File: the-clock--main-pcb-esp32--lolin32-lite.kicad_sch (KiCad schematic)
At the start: 14 parts, among them J1 Conn_01x04, SW1 SW_Push, SW2 SW_Push, SW3 SW_Push, SW4 SW_Push

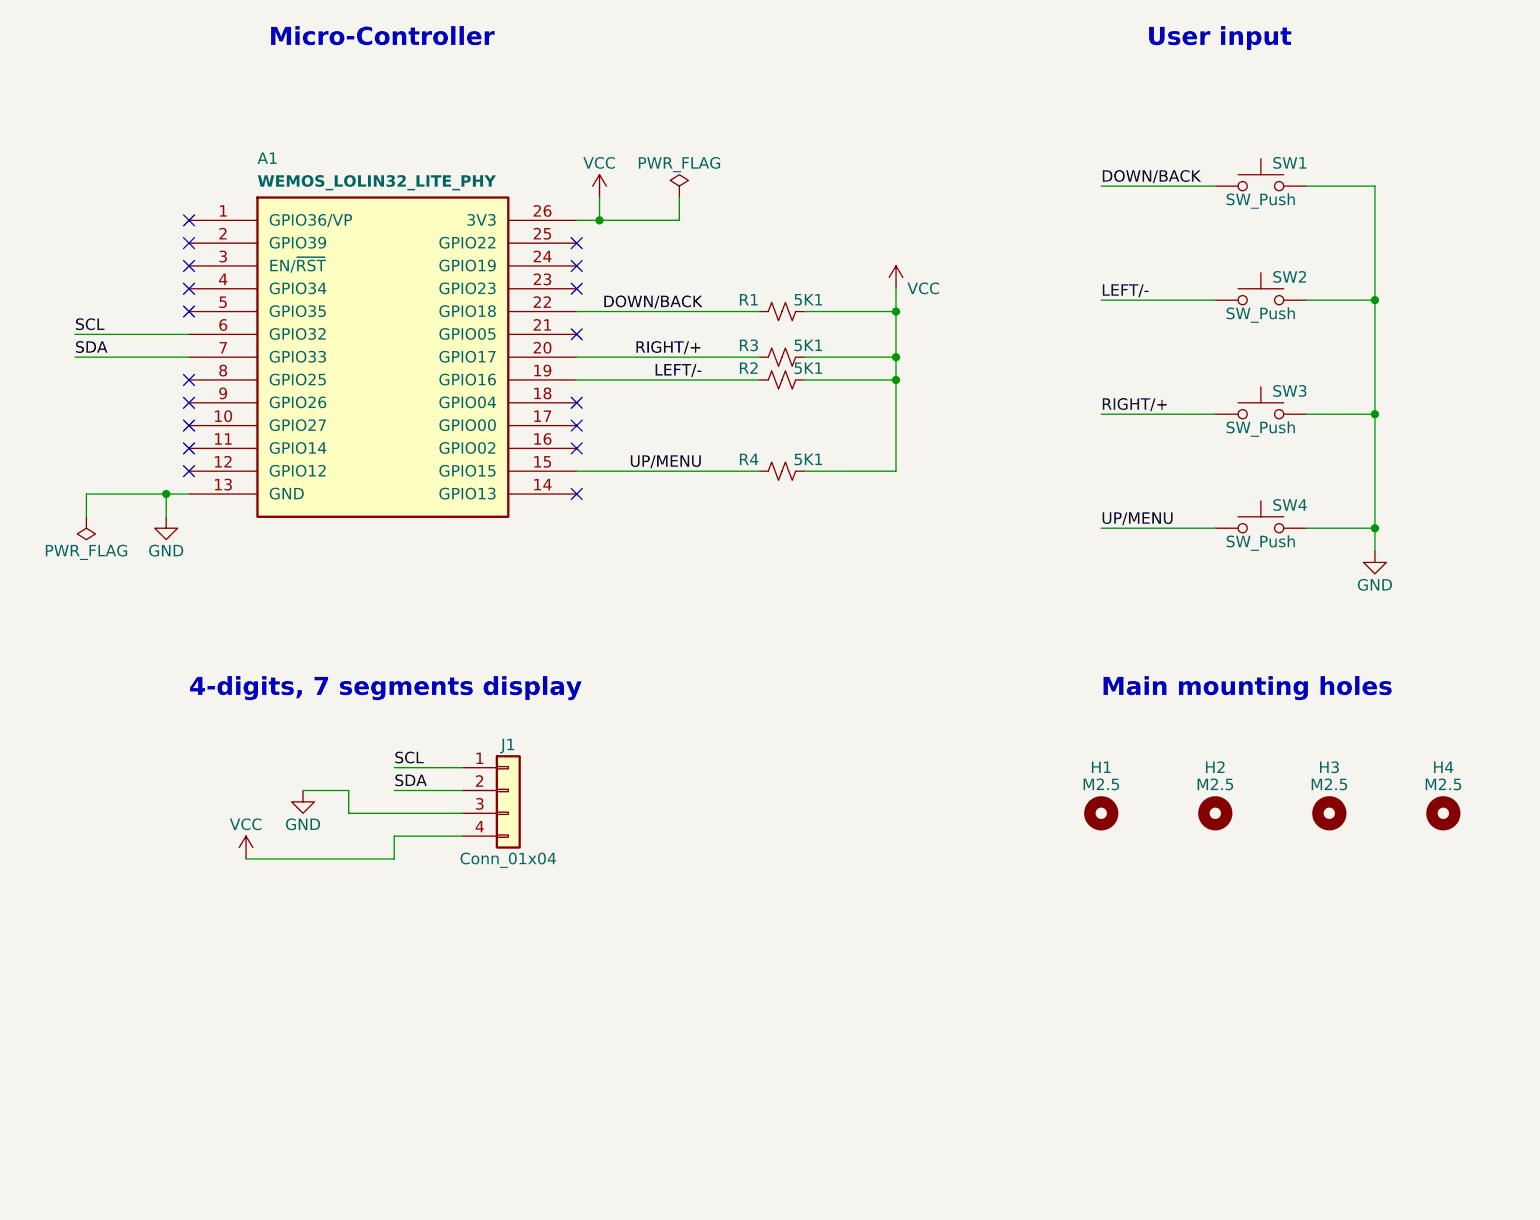
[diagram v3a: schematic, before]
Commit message: provision ambient light sensor
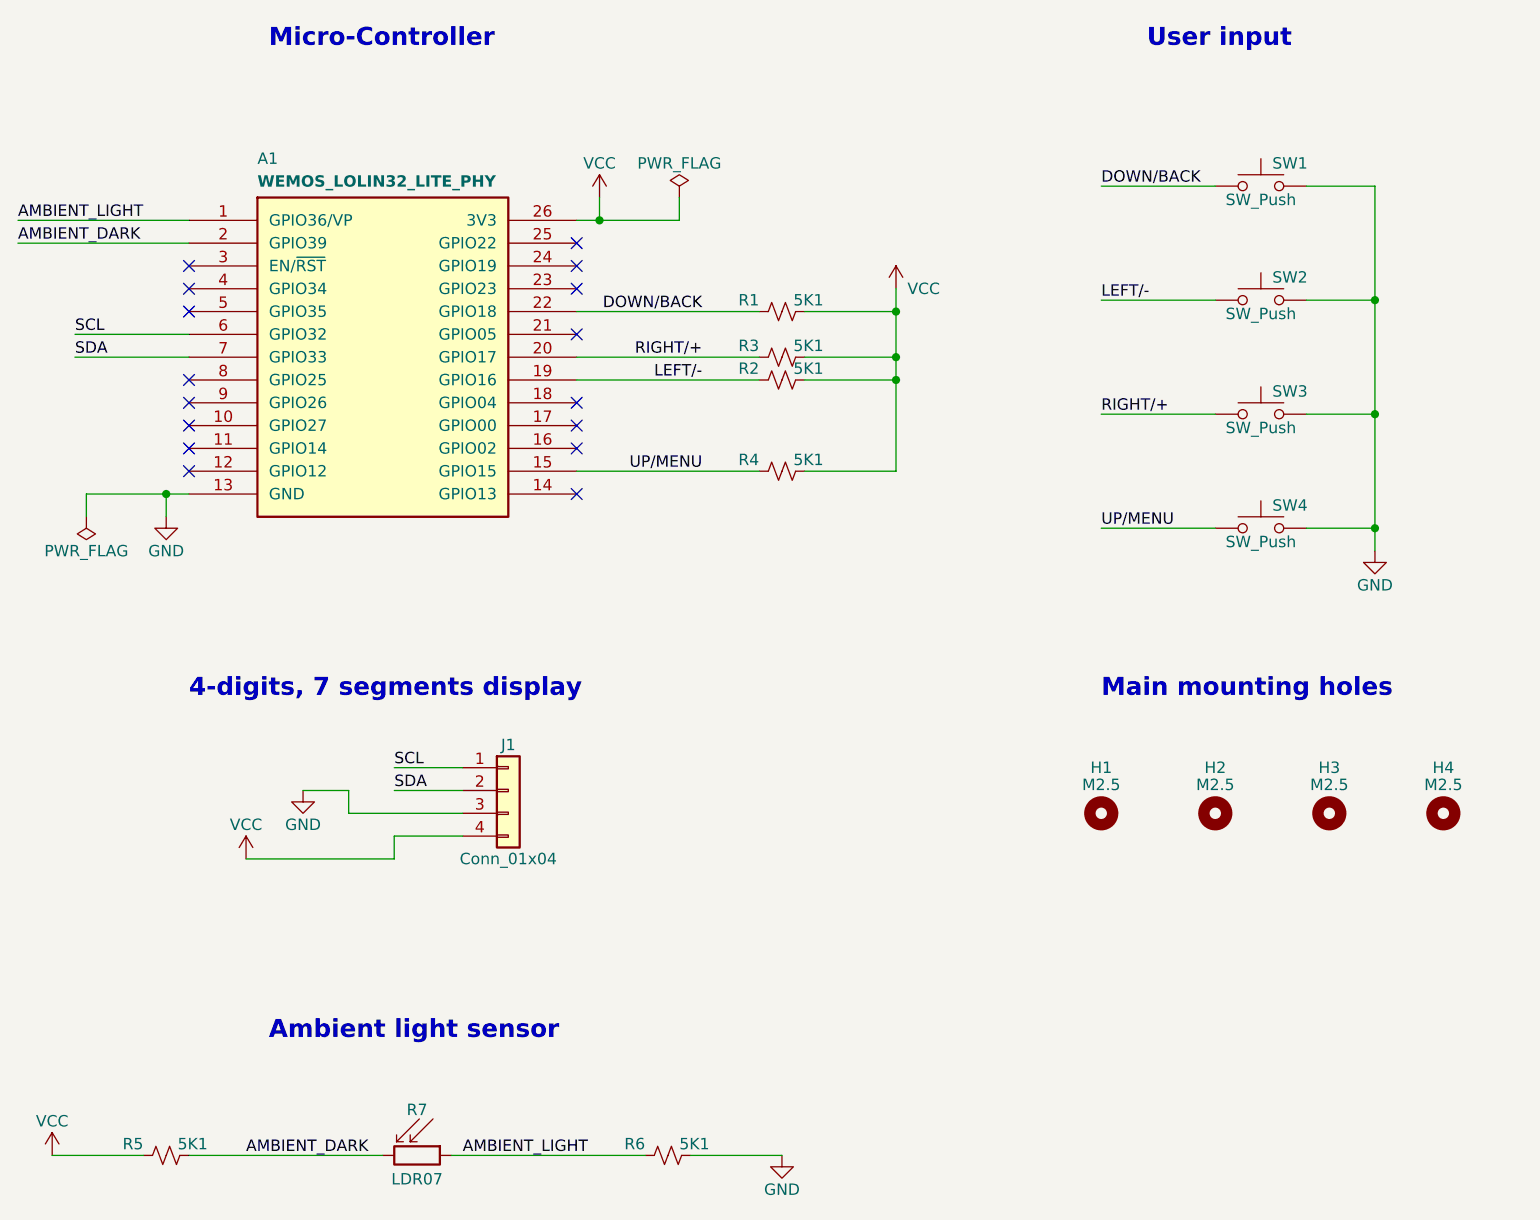
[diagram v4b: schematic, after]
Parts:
- added R5, R6: 5K1, commons-passives_THT:Passive_THT_resistor_W2.54mm_L10.16mm, symbol Device:R_Small_US
- added R7: LDR07, OptoDevice:R_LDR_5.1x4.3mm_P3.4mm_Vertical, symbol Sensor_Optical:LDR07
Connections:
- net GND: now also R6.2
- net VCC: now also R5.1
- net AMBIENT_LIGHT: now reaches A1.1 (GPIO36/VP)
- net AMBIENT_LIGHT: now also R6.1, R7.1
- net AMBIENT_DARK: now reaches A1.2 (GPIO39)
- net AMBIENT_DARK: now also R5.2, R7.2
- no-connect marks 18 -> 16
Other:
- note added: "Ambient light sensor"
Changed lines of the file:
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@@
   (no_connect (at 81.28 60.96))
   (no_connect (at 38.1 68.58))
-  (no_connect (at 38.1 50.8))
   (no_connect (at 81.28 71.12))
   (no_connect (at 38.1 55.88))
   (no_connect (at 38.1 76.2))
   (no_connect (at 81.28 53.34))
-  (no_connect (at 38.1 48.26))
   (no_connect (at 81.28 78.74))
   (no_connect (at 81.28 73.66))
@@
     (stroke (width 0) (type default))
   )
+  (wire (pts (xy 38.1 152.4) (xy 59.69 152.4))
+    (stroke (width 0) (type default))
+  )
   (wire (pts (xy 60.96 111.76) (xy 68.58 111.76))
     (stroke (width 0) (type default))
@@
     (stroke (width 0) (type default))
   )
+  (wire (pts (xy 19.05 50.8) (xy 38.1 50.8))
+    (stroke (width 0) (type default))
+  )
   (wire (pts (xy 170.18 69.85) (xy 170.18 57.15))
     (stroke (width 0) (type default))
@@
     (stroke (width 0) (type default))
   )
+  (wire (pts (xy 67.31 152.4) (xy 88.9 152.4))
+    (stroke (width 0) (type default))
+  )
   (wire (pts (xy 162.56 44.45) (xy 170.18 44.45))
     (stroke (width 0) (type default))
   )
+  (wire (pts (xy 22.86 152.4) (xy 33.02 152.4))
+    (stroke (width 0) (type default))
+  )
   (wire (pts (xy 162.56 69.85) (xy 170.18 69.85))
     (stroke (width 0) (type default))
@@
     (stroke (width 0) (type default))
   )
+  (wire (pts (xy 19.05 48.26) (xy 38.1 48.26))
+    (stroke (width 0) (type default))
+  )
   (wire (pts (xy 106.68 58.42) (xy 116.84 58.42))
     (stroke (width 0) (type default))
   )
   (wire (pts (xy 26.67 81.28) (xy 26.67 78.74))
+    (stroke (width 0) (type default))
+  )
+  (wire (pts (xy 93.98 152.4) (xy 104.14 152.4))
     (stroke (width 0) (type default))
   )
@@
     (effects (font (size 2 2) (thickness 0.4) bold) (justify left bottom))
   )
+  (text "Ambient light sensor" (at 46.99 139.7 0)
+    (effects (font (size 2 2) (thickness 0.4) bold) (justify left bottom))
+  )
   (text "User input" (at 144.78 29.21 0)
     (effects (font (size 2 2) (thickness 0.4) bold) (justify left bottom))
@@
     (effects (font (size 1.27 1.27)) (justify left bottom))
   )
+  (label "AMBIENT_LIGHT" (at 68.58 152.4 0) (fields_autoplaced)
+    (effects (font (size 1.27 1.27)) (justify left bottom))
+  )
   (label "SCL" (at 60.96 109.22 0) (fields_autoplaced)
     (effects (font (size 1.27 1.27)) (justify left bottom))
@@
   )
   (label "SDA" (at 60.96 111.76 0) (fields_autoplaced)
+    (effects (font (size 1.27 1.27)) (justify left bottom))
+  )
+  (label "AMBIENT_DARK" (at 19.05 50.8 0) (fields_autoplaced)
     (effects (font (size 1.27 1.27)) (justify left bottom))
   )
@@
     (effects (font (size 1.27 1.27)) (justify left bottom))
   )
+  (label "AMBIENT_DARK" (at 44.45 152.4 0) (fields_autoplaced)
+    (effects (font (size 1.27 1.27)) (justify left bottom))
+  )
+  (label "AMBIENT_LIGHT" (at 19.05 48.26 0) (fields_autoplaced)
+    (effects (font (size 1.27 1.27)) (justify left bottom))
+  )
   (symbol (lib_id "power:PWR_FLAG") (at 92.71 45.72 0) (unit 1)
     (in_bom yes) (on_board yes) (dnp no)
@@
         (path "/dfc91cd7-0548-4b37-8d64-94d7833ed062"
           (reference "H2") (unit 1)
+        )
+      )
+    )
+  )
+  (symbol (lib_id "power:VCC") (at 22.86 152.4 0) (unit 1)
+    (in_bom yes) (on_board yes) (dnp no)
+    (property "Reference" "#PWR07" (at 22.86 156.21 0)
+      (effects (font (size 1.27 1.27)) hide)
+    )
+    (property "Value" "VCC" (at 22.86 148.59 0)
+      (effects (font (size 1.27 1.27)))
+    )
+    (property "Footprint" "" (at 22.86 152.4 0)
+      (effects (font (size 1.27 1.27)) hide)
+    )
+    (property "Datasheet" "" (at 22.86 152.4 0)
+      (effects (font (size 1.27 1.27)) hide)
+    )
+    (pin "1")
+    (instances
+      (project "the-clock--main-pcb-esp32--lolin32-lite"
+        (path "/dfc91cd7-0548-4b37-8d64-94d7833ed062"
+          (reference "#PWR07") (unit 1)
+        )
+      )
+    )
+  )
+  (symbol (lib_id "Device:R_Small_US") (at 35.56 152.4 90) (unit 1)
+    (in_bom yes) (on_board yes) (dnp no)
+    (property "Reference" "R5" (at 33.02 151.13 90)
+      (effects (font (size 1.27 1.27)) (justify left))
+    )
+    (property "Value" "5K1" (at 36.83 151.13 90)
+      (effects (font (size 1.27 1.27)) (justify right))
+    )
+    (property "Footprint" "commons-passives_THT:Passive_THT_resistor_W2.54mm_L10.16mm" (at 35.56 152.4 0)
+      (effects (font (size 1.27 1.27)) hide)
+    )
+    (property "Datasheet" "~" (at 35.56 152.4 0)
+      (effects (font (size 1.27 1.27)) hide)
+    )
+    (pin "1")
+    (pin "2")
+    (instances
+      (project "the-clock--main-pcb-esp32--lolin32-lite"
+        (path "/dfc91cd7-0548-4b37-8d64-94d7833ed062"
+          (reference "R5") (unit 1)
+        )
+      )
+    )
+  )
+  (symbol (lib_id "Device:R_Small_US") (at 91.44 152.4 90) (unit 1)
+    (in_bom yes) (on_board yes) (dnp no)
+    (property "Reference" "R6" (at 88.9 151.13 90)
+      (effects (font (size 1.27 1.27)) (justify left))
+    )
+    (property "Value" "5K1" (at 92.71 151.13 90)
+      (effects (font (size 1.27 1.27)) (justify right))
+    )
+    (property "Footprint" "commons-passives_THT:Passive_THT_resistor_W2.54mm_L10.16mm" (at 91.44 152.4 0)
+      (effects (font (size 1.27 1.27)) hide)
+    )
+    (property "Datasheet" "~" (at 91.44 152.4 0)
+      (effects (font (size 1.27 1.27)) hide)
+    )
+    (pin "1")
+    (pin "2")
+    (instances
+      (project "the-clock--main-pcb-esp32--lolin32-lite"
+        (path "/dfc91cd7-0548-4b37-8d64-94d7833ed062"
+          (reference "R6") (unit 1)
         )
       )
@@
     )
   )
+  (symbol (lib_id "power:GND") (at 104.14 152.4 0) (unit 1)
+    (in_bom yes) (on_board yes) (dnp no)
+    (property "Reference" "#PWR08" (at 104.14 158.75 0)
+      (effects (font (size 1.27 1.27)) hide)
+    )
+    (property "Value" "GND" (at 104.14 156.21 0)
+      (effects (font (size 1.27 1.27)))
+    )
+    (property "Footprint" "" (at 104.14 152.4 0)
+      (effects (font (size 1.27 1.27)) hide)
+    )
+    (property "Datasheet" "" (at 104.14 152.4 0)
+      (effects (font (size 1.27 1.27)) hide)
+    )
+    (pin "1")
+    (instances
+      (project "the-clock--main-pcb-esp32--lolin32-lite"
+        (path "/dfc91cd7-0548-4b37-8d64-94d7833ed062"
+          (reference "#PWR08") (unit 1)
+        )
+      )
+    )
+  )
   (symbol (lib_id "Device:R_Small_US") (at 104.14 63.5 90) (unit 1)
     (in_bom yes) (on_board yes) (dnp no)
@@
         )
       )
+    )
+  )
+  (symbol (lib_id "Sensor_Optical:LDR07") (at 63.5 152.4 270) (unit 1)
+    (in_bom yes) (on_board yes) (dnp no)
+    (property "Reference" "R7" (at 63.5 147.32 90)
+      (effects (font (size 1.27 1.27)))
+    )
+    (property "Value" "LDR07" (at 63.5 154.305 90)
+      (effects (font (size 1.27 1.27)) (justify top))
+    )
+    (property "Footprint" "OptoDevice:R_LDR_5.1x4.3mm_P3.4mm_Vertical" (at 63.5 156.845 90)
+      (effects (font (size 1.27 1.27)) hide)
+    )
+    (property "Datasheet" "http://www.tme.eu/de/Document/f2e3ad76a925811312d226c31da4cd7e/LDR07.pdf" (at 62.23 152.4 0)
+      (effects (font (size 1.27 1.27)) hide)
+    )
+    (pin "1")
+    (pin "2")
+    (instances
+      (project "the-clock--main-pcb-esp32--lolin32-lite"
+        (path "/dfc91cd7-0548-4b37-8d64-94d7833ed062"
+          (reference "R7") (unit 1)
+        )
+      )
